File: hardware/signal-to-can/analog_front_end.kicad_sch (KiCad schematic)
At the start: 5 parts

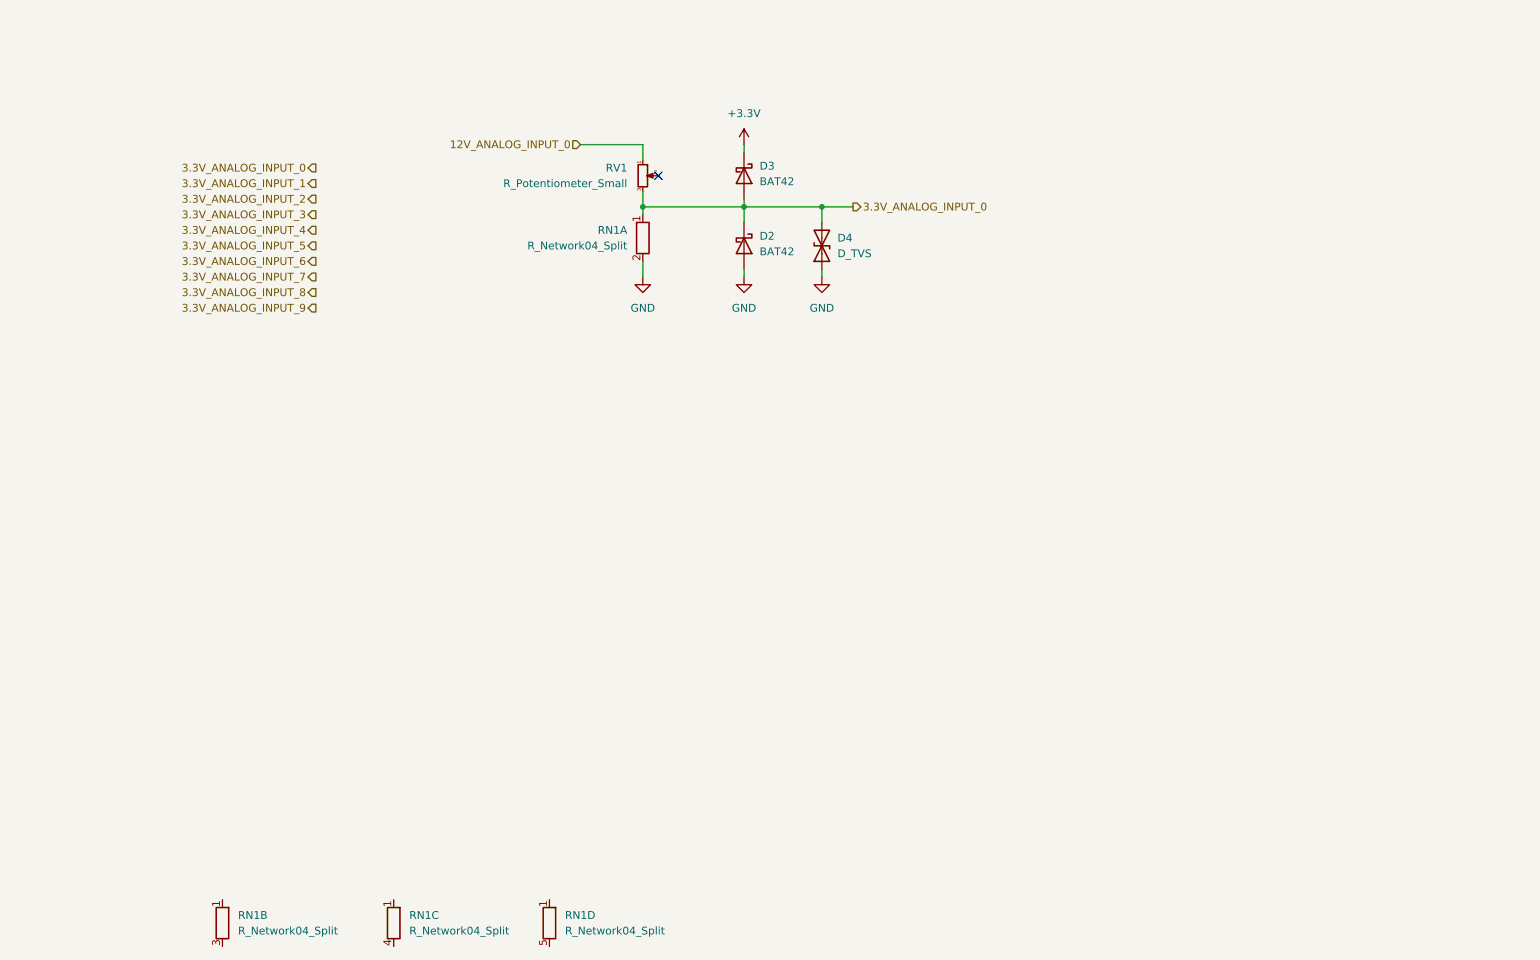
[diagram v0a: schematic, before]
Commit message: AFE, power supply, connector
Ready for PCB layout
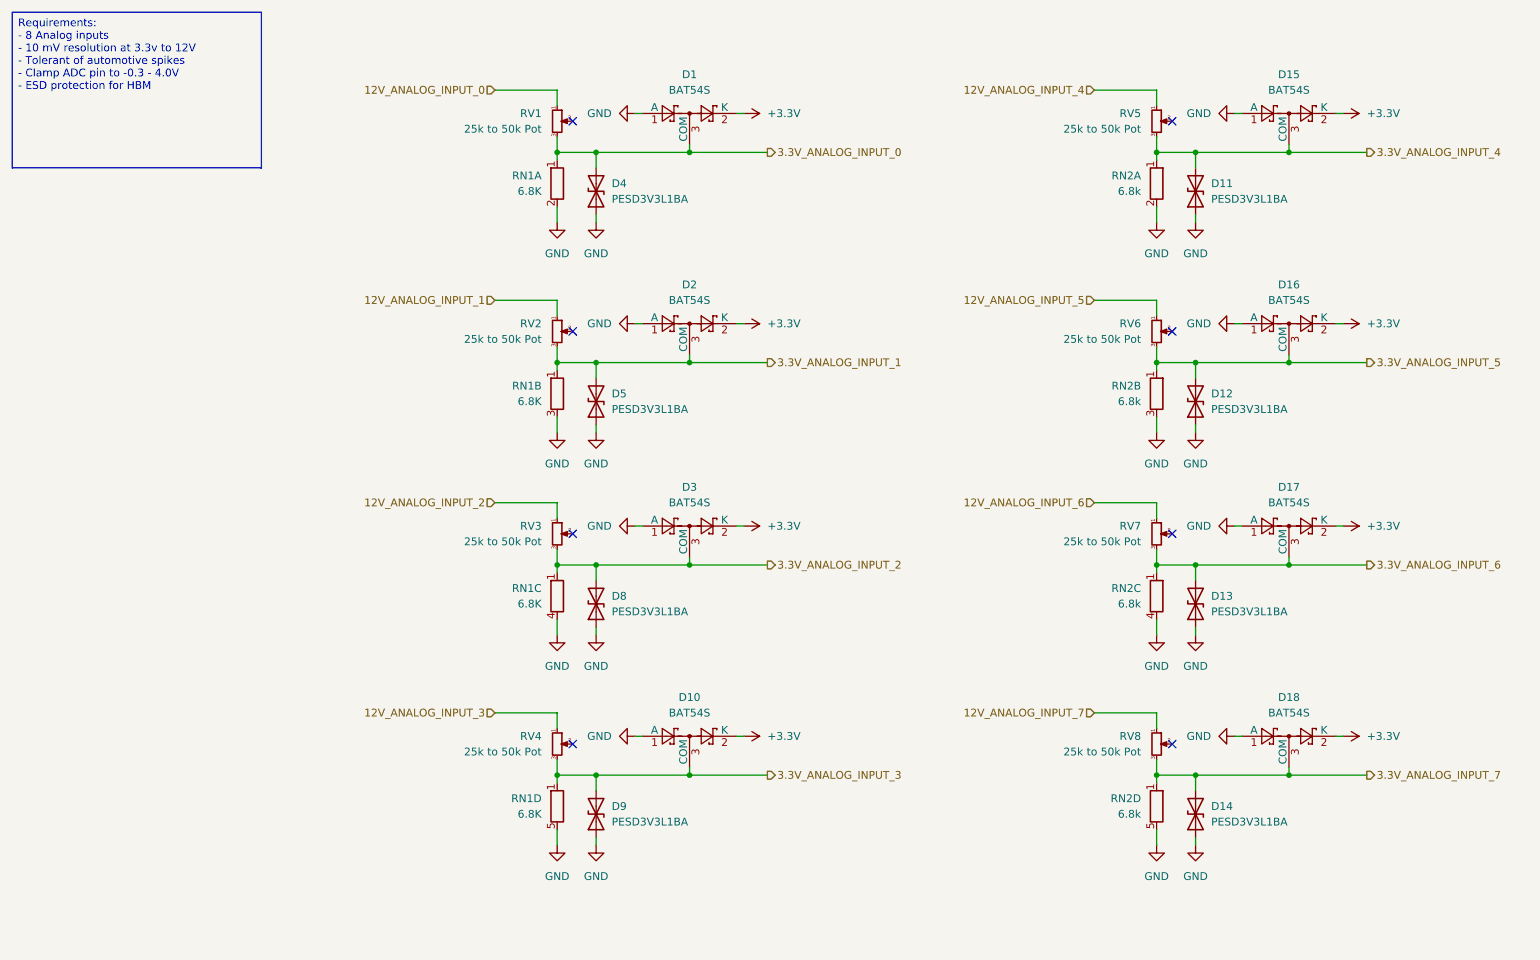
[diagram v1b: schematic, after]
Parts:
- removed D2, D3: BAT42, Diode_THT:D_DO-35_SOD27_P7.62mm_Horizontal, symbol Diode:BAT42
- added D1, D10, D15, D16, D17, D18, D2, D3: BAT54S, Package_TO_SOT_SMD:SOT-23, symbol Diode:BAT54S
- added D11, D12, D13, D14, D5, D8, D9: PESD3V3L1BA, symbol Device:D_TVS
- added RN2: 6.8k, Resistor_THT:R_Array_SIP5, symbol Device:R_Network04_Split
- added RV2, RV3, RV4, RV5, RV6, RV7, RV8: 25k to 50k Pot, symbol Device:R_Potentiometer_Small
- D4: value D_TVS -> PESD3V3L1BA
- RN1: value R_Network04_Split -> 6.8K
- RV1: value R_Potentiometer_Small -> 25k to 50k Pot
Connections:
- net +3.3V: now also D1.2 (K), D10.2 (K), D15.2 (K), D16.2 (K), D17.2 (K), D18.2 (K), D2.2 (K), D3.2 (K)
- net 3.3V_ANALOG_INPUT_0: now also D1.3 (COM)
- net 3.3V_ANALOG_INPUT_1: now also RN1.1 (R1), D2.3 (COM), D5.2 (A2), RV2.3
- net 3.3V_ANALOG_INPUT_2: now also RN1.1 (R1), D3.3 (COM), D8.2 (A2), RV3.3
- net 3.3V_ANALOG_INPUT_3: now also RN1.1 (R1), D10.3 (COM), D9.2 (A2), RV4.3
- net 3.3V_ANALOG_INPUT_4: now also D11.2 (A2), D15.3 (COM), RN2.1 (R1), RV5.3
- net 3.3V_ANALOG_INPUT_5: now also D12.2 (A2), D16.3 (COM), RN2.1 (R1), RV6.3
- net 3.3V_ANALOG_INPUT_6: now also D13.2 (A2), D17.3 (COM), RN2.1 (R1), RV7.3
- net 3.3V_ANALOG_INPUT_7: now also D14.2 (A2), D18.3 (COM), RN2.1 (R1), RV8.3
- net GND: now also RN1.3 (R2.2), RN1.4 (R3.2), RN1.5 (R4.2), D1.1 (A), D10.1 (A), D11.1 (A1), D12.1 (A1), D13.1 (A1), D14.1 (A1), D15.1 (A), D16.1 (A), D17.1 (A), D18.1 (A), D2.1 (A), D3.1 (A), D5.1 (A1), D8.1 (A1), D9.1 (A1), RN2.2 (R1.2), RN2.3 (R2.2), RN2.4 (R3.2), RN2.5 (R4.2)
- new net 12V_ANALOG_INPUT_1: RV2.1
- new net 12V_ANALOG_INPUT_2: RV3.1
- new net 12V_ANALOG_INPUT_3: RV4.1
- new net 12V_ANALOG_INPUT_4: RV5.1
- new net 12V_ANALOG_INPUT_5: RV6.1
- new net 12V_ANALOG_INPUT_6: RV7.1
- new net 12V_ANALOG_INPUT_7: RV8.1
- no-connect marks 1 -> 8
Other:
- moved on the sheet: D4, RN1A, RN1B, RN1C, RN1D, RV1

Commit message: 1st rev PCB layout
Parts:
- removed RN1: 6.8K, Resistor_THT:R_Array_SIP5, symbol Device:R_Network04_Split
- removed RN2: 6.8k, Resistor_THT:R_Array_SIP5, symbol Device:R_Network04_Split
- added R10, R11, R12, R13, R6, R7, R8, R9: 6.8k, Resistor_SMD:R_0603_1608Metric, symbol Device:R
- D13: renamed from D11; footprint (none) -> Diode_SMD:D_SOD-323
- D14: renamed from D12; footprint (none) -> Diode_SMD:D_SOD-323
- D15: renamed from D13; footprint (none) -> Diode_SMD:D_SOD-323
- D16: renamed from D14; footprint (none) -> Diode_SMD:D_SOD-323
- D5: renamed from D4; footprint (none) -> Diode_SMD:D_SOD-323
- D6: renamed from D5; footprint (none) -> Diode_SMD:D_SOD-323
- D7: renamed from D8; footprint (none) -> Diode_SMD:D_SOD-323
- D8: renamed from D9; footprint (none) -> Diode_SMD:D_SOD-323
- RV1, RV2, RV3, RV4, RV5, RV6, RV7, RV8: value 25k to 50k Pot -> 3314G-1-503E; footprint (none) -> Potentiometer_SMD:Potentiometer_Bourns_3314G_Vertical
- renumbered D2 to D10, D3 to D11, D10 to D12, D15 to D17, D16 to D18, D17 to D19, D18 to D20, D1 to D9
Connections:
- net 3.3V_ANALOG_INPUT_0: now also R6.1
- net 3.3V_ANALOG_INPUT_1: now also R7.1
- net 3.3V_ANALOG_INPUT_2: now also R8.1
- net 3.3V_ANALOG_INPUT_3: now also R9.1
- net 3.3V_ANALOG_INPUT_4: now also R10.1
- net 3.3V_ANALOG_INPUT_5: now also R11.1
- net 3.3V_ANALOG_INPUT_6: now also R12.1
- net 3.3V_ANALOG_INPUT_7: now also R13.1
- net GND: now also R10.2, R11.2, R12.2, R13.2, R6.2, R7.2, R8.2, R9.2
- net +3.3V renamed +3V3
